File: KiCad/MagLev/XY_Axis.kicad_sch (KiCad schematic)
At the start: 36 parts, among them Q1 ZX5T851GTA, Q2 ZX5T1951GTA, Q3 ZX5T851GTA, Q4 ZX5T1951GTA, U1 LM324

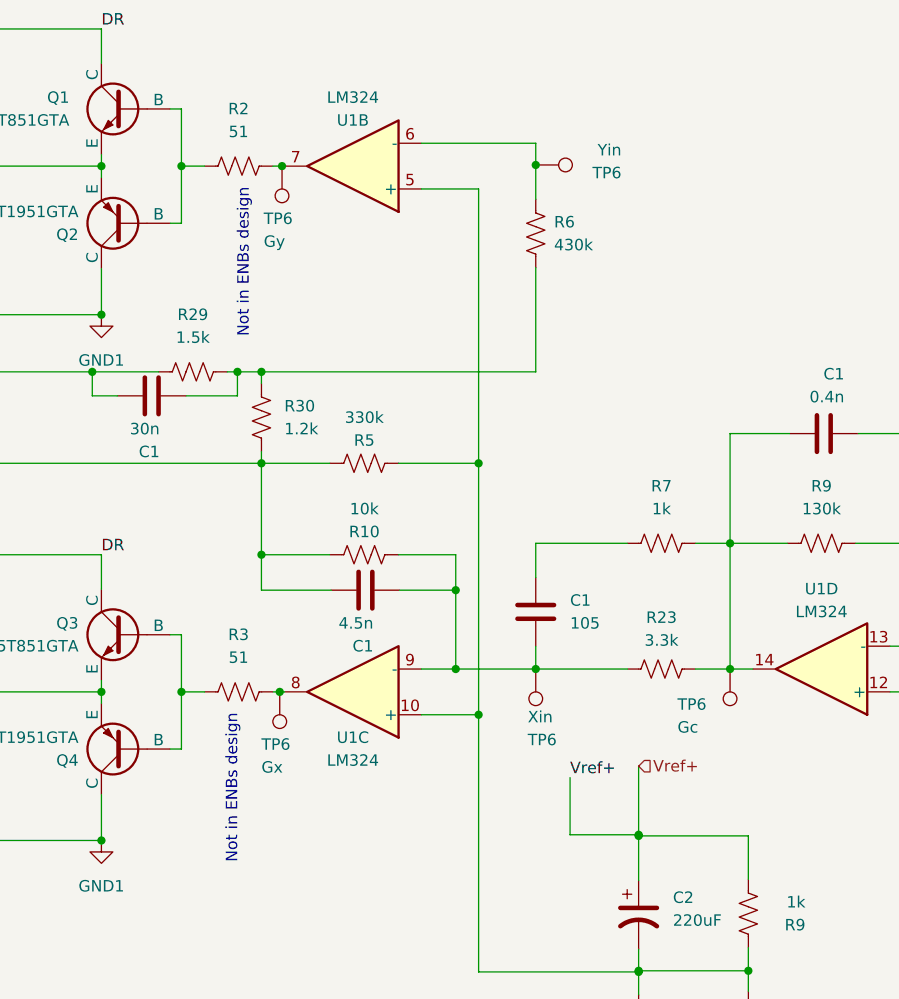
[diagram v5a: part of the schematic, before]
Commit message: Route TPs, increase power trace size.
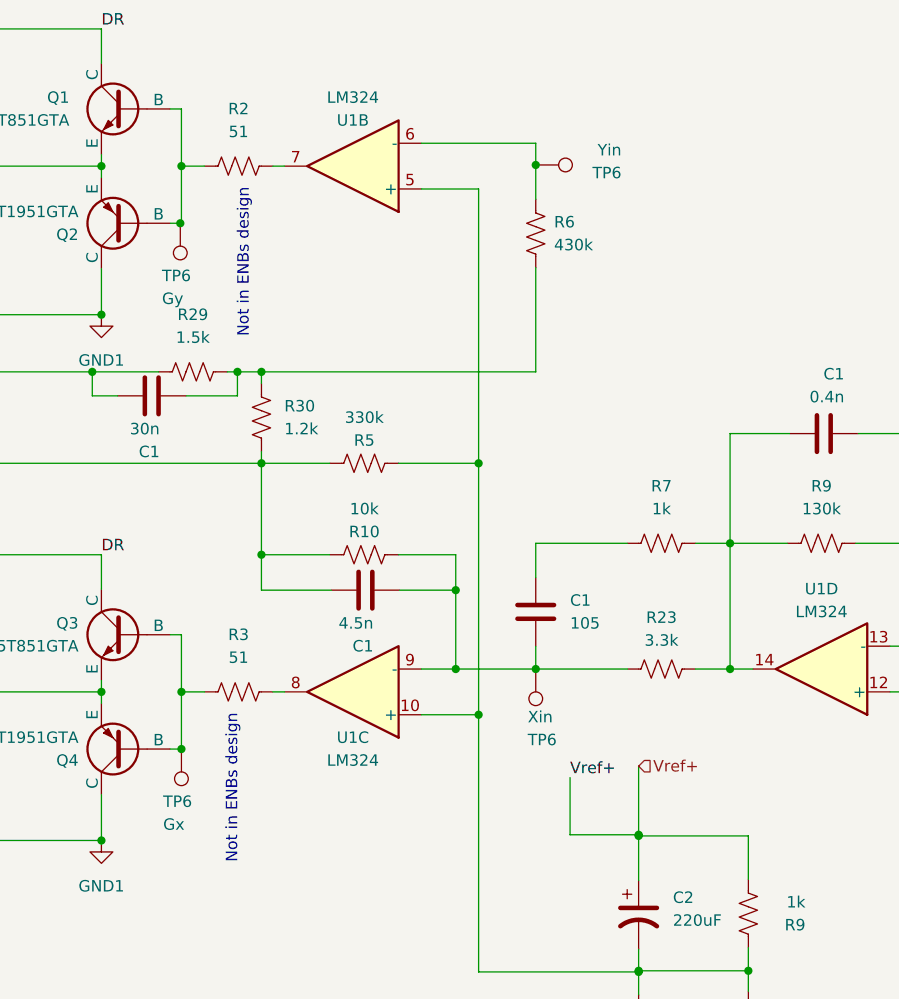
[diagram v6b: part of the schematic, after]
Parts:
- removed TP6: Gc, TestPoint:TestPoint_Pad_D2.0mm, symbol Connector:TestPoint
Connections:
- net at Q3.2 (B), Q4.2 (B), R3.1: now also TP6.1
- net at Q1.2 (B), Q2.2 (B), R2.1: now also TP6.1
- net at R2.2, U1.7: no longer TP6.1
- net at R3.2, U1.8: no longer TP6.1
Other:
- moved on the sheet: TP6
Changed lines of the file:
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@@
     (company "Kevin Dueck")
   )
+  (junction (at 121.666 111.252) (diameter 0) (color 0 0 0 0)
+  )
   (junction (at 38.608 56.642) (diameter 0) (color 0 0 0 0)
   )
@@
   (junction (at 112.776 46.482) (diameter 0) (color 0 0 0 0)
   )
+  (junction (at 121.539 52.832) (diameter 0) (color 0 0 0 0)
+  )
   (junction (at 81.026 46.482) (diameter 0) (color 0 0 0 0)
   )
@@
   (junction (at 112.776 104.902) (diameter 0) (color 0 0 0 0)
   )
-  (junction (at 132.842 46.482) (diameter 0) (color 0 0 0 0)
-  )
   (junction (at 81.026 104.902) (diameter 0) (color 0 0 0 0)
   )
@@
   )
   (junction (at 154.686 79.502) (diameter 0) (color 0 0 0 0)
-  )
-  (junction (at 132.588 104.902) (diameter 0) (color 0 0 0 0)
   )
   (junction (at 172.466 120.904) (diameter 0) (color 0 0 0 0)
@@
     (stroke (width 0) (type default))
   )
-  (wire (pts (xy 133.096 46.482) (xy 132.842 46.482))
-    (stroke (width 0) (type default))
-  )
   (wire (pts (xy 182.626 88.392) (xy 188.976 88.392))
     (stroke (width 0) (type default))
@@
     (stroke (width 0) (type default))
   )
-  (wire (pts (xy 121.666 52.832) (xy 120.396 52.832))
+  (wire (pts (xy 121.666 52.832) (xy 121.539 52.832))
     (stroke (width 0) (type default))
   )
@@
     (stroke (width 0) (type default))
   )
-  (wire (pts (xy 133.096 104.902) (xy 132.588 104.902))
-    (stroke (width 0) (type default))
-  )
   (wire (pts (xy 172.466 147.574) (xy 172.466 151.257))
     (stroke (width 0) (type default))
@@
     (stroke (width 0) (type default))
   )
-  (wire (pts (xy 132.588 104.902) (xy 131.826 104.902))
+  (wire (pts (xy 131.826 104.902) (xy 133.096 104.902))
     (stroke (width 0) (type default))
   )
@@
     (stroke (width 0) (type default))
   )
+  (wire (pts (xy 121.539 52.832) (xy 120.396 52.832))
+    (stroke (width 0) (type default))
+  )
   (wire (pts (xy 111.76 72.009) (xy 114.554 72.009))
     (stroke (width 0) (type default))
@@
     (stroke (width 0) (type default))
   )
-  (wire (pts (xy 132.842 46.482) (xy 131.826 46.482))
+  (wire (pts (xy 131.826 46.482) (xy 133.096 46.482))
     (stroke (width 0) (type default))
   )
@@
     )
   )
-  (symbol (lib_id "Connector:TestPoint") (at 132.842 46.482 180) (unit 1)
-    (in_bom yes) (on_board yes) (dnp no)
-    (property "Reference" "TP6" (at 130.81 52.324 0)
+  (symbol (lib_id "Connector:TestPoint") (at 121.539 52.832 180) (unit 1)
+    (in_bom yes) (on_board yes) (dnp no)
+    (property "Reference" "TP6" (at 119.507 58.674 0)
       (effects (font (size 1.27 1.27)) (justify right))
     )
-    (property "Value" "Gy" (at 130.81 54.864 0)
+    (property "Value" "Gy" (at 119.507 61.214 0)
       (effects (font (size 1.27 1.27)) (justify right))
     )
-    (property "Footprint" "TestPoint:TestPoint_Pad_D2.0mm" (at 127.762 46.482 0)
-      (effects (font (size 1.27 1.27)) hide)
-    )
-    (property "Datasheet" "~" (at 127.762 46.482 0)
+    (property "Footprint" "TestPoint:TestPoint_Pad_D2.0mm" (at 116.459 52.832 0)
+      (effects (font (size 1.27 1.27)) hide)
+    )
+    (property "Datasheet" "~" (at 116.459 52.832 0)
       (effects (font (size 1.27 1.27)) hide)
     )
@@
         (path "/5eab7e8b-54e1-47d0-9dc3-1e7c3fa2f560/7df46fb0-abf8-474a-ba30-7ff9455482b6"
           (reference "TP23") (unit 1)
-        )
-      )
-    )
-  )
-  (symbol (lib_id "Connector:TestPoint") (at 182.626 102.362 180) (unit 1)
-    (in_bom yes) (on_board yes) (dnp no)
-    (property "Reference" "TP6" (at 176.784 106.299 0)
-      (effects (font (size 1.27 1.27)) (justify right))
-    )
-    (property "Value" "Gc" (at 176.784 108.839 0)
-      (effects (font (size 1.27 1.27)) (justify right))
-    )
-    (property "Footprint" "TestPoint:TestPoint_Pad_D2.0mm" (at 177.546 102.362 0)
-      (effects (font (size 1.27 1.27)) hide)
-    )
-    (property "Datasheet" "~" (at 177.546 102.362 0)
-      (effects (font (size 1.27 1.27)) hide)
-    )
-    (pin "1")
-    (instances
-      (project "MagLev"
-        (path "/5eab7e8b-54e1-47d0-9dc3-1e7c3fa2f560"
-          (reference "TP6") (unit 1)
-        )
-        (path "/5eab7e8b-54e1-47d0-9dc3-1e7c3fa2f560/1b1a7f40-4880-4dc8-87d1-1ed1d4fb8d1e"
-          (reference "TP11") (unit 1)
-        )
-        (path "/5eab7e8b-54e1-47d0-9dc3-1e7c3fa2f560/7df46fb0-abf8-474a-ba30-7ff9455482b6"
-          (reference "TP12") (unit 1)
         )
       )
@@
     )
   )
-  (symbol (lib_id "Connector:TestPoint") (at 132.588 104.902 180) (unit 1)
-    (in_bom yes) (on_board yes) (dnp no)
-    (property "Reference" "TP6" (at 130.556 110.744 0)
+  (symbol (lib_id "Connector:TestPoint") (at 121.666 111.252 180) (unit 1)
+    (in_bom yes) (on_board yes) (dnp no)
+    (property "Reference" "TP6" (at 119.634 117.094 0)
       (effects (font (size 1.27 1.27)) (justify right))
     )
-    (property "Value" "Gx" (at 130.556 113.284 0)
+    (property "Value" "Gx" (at 119.634 119.634 0)
       (effects (font (size 1.27 1.27)) (justify right))
     )
-    (property "Footprint" "TestPoint:TestPoint_Pad_D2.0mm" (at 127.508 104.902 0)
-      (effects (font (size 1.27 1.27)) hide)
-    )
-    (property "Datasheet" "~" (at 127.508 104.902 0)
-      (effects (font (size 1.27 1.27)) hide)
-    )
+    (property "Footprint" "TestPoint:TestPoint_Pad_D2.0mm" (at 116.586 111.252 0)
+      (effects (font (size 1.27 1.27)) hide)
+    )
+    (property "Datasheet" "~" (at 116.586 111.252 0)
+      (effects (font (size 1.27 1.27)) hide)
+    )

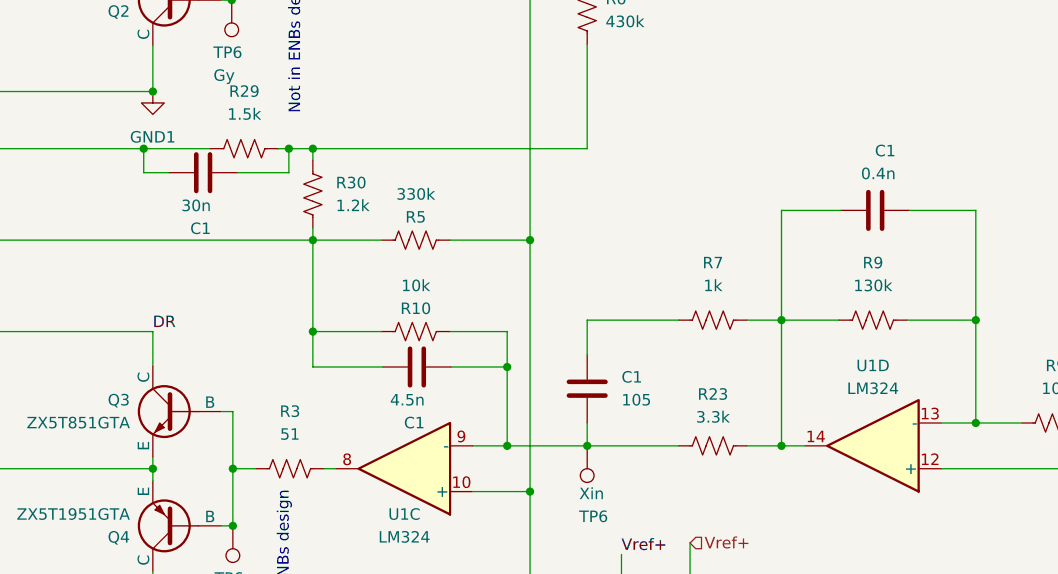
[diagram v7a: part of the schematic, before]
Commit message: Set LED bias resistors. Move MCU status LEDs to PWM pins.
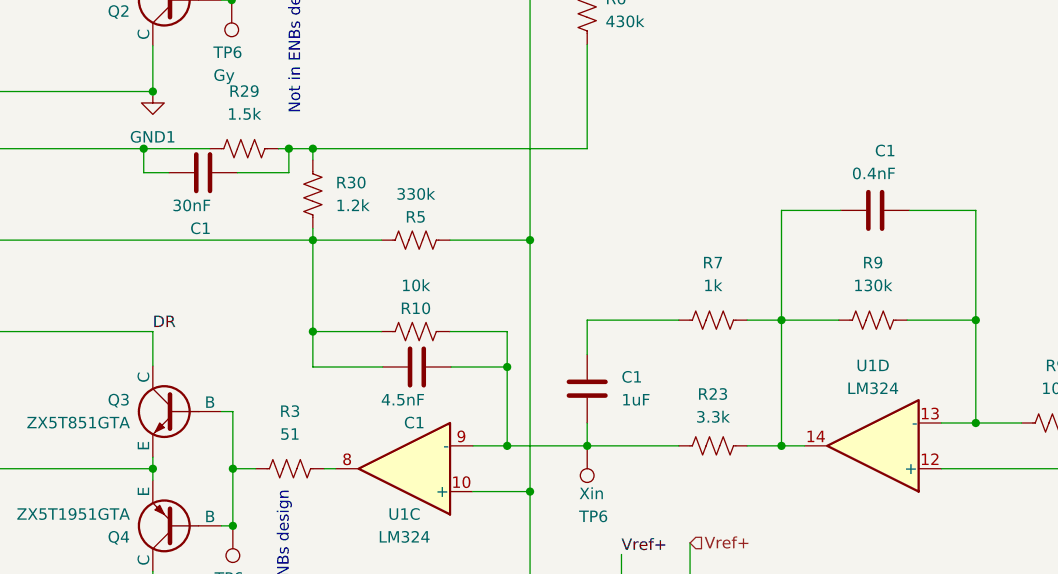
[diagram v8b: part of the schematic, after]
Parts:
- C1: value 105 -> 1uF
- C1: value 30n -> 30nF
- C1: value 0.4n -> 0.4nF
- C1: value 4.5n -> 4.5nF
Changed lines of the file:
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@@
       (effects (font (size 1.27 1.27)) (justify left))
     )
-    (property "Value" "105" (at 164.846 97.282 0)
+    (property "Value" "1uF" (at 164.846 97.282 0)
       (effects (font (size 1.27 1.27)) (justify left))
     )
@@
       (effects (font (size 1.27 1.27)) (justify left))
     )
-    (property "Value" "30n" (at 119.253 75.692 90)
+    (property "Value" "30nF" (at 119.253 75.692 90)
       (effects (font (size 1.27 1.27)) (justify left))
     )
@@
       (effects (font (size 1.27 1.27)) (justify left))
     )
-    (property "Value" "0.4n" (at 195.326 72.136 90)
+    (property "Value" "0.4nF" (at 195.326 72.136 90)
       (effects (font (size 1.27 1.27)) (justify left))
     )
@@
       (effects (font (size 1.27 1.27)) (justify left))
     )
-    (property "Value" "4.5n" (at 143.002 97.282 90)
-      (effects (font (size 1.27 1.27)) (justify left))
-    )
+    (property "Value" "4.5nF" (at 143.002 97.282 90)
+      (effects (font (size 1.27 1.27)) (justify left))
+    )
